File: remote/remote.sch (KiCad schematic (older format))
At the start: 57 parts, among them J1 Conn_01x04, J2 Conn_01x05, Q1 AO3401A, Q2 AO3401A, Q3 AO3401A, Q4 AO3401A, SW1 SW_Push, SW2 SW_Push, SW3 SW_Push, SW4 SW_Push, U1 STM32F030F4Px, U2 RFM69CW-915MHZ

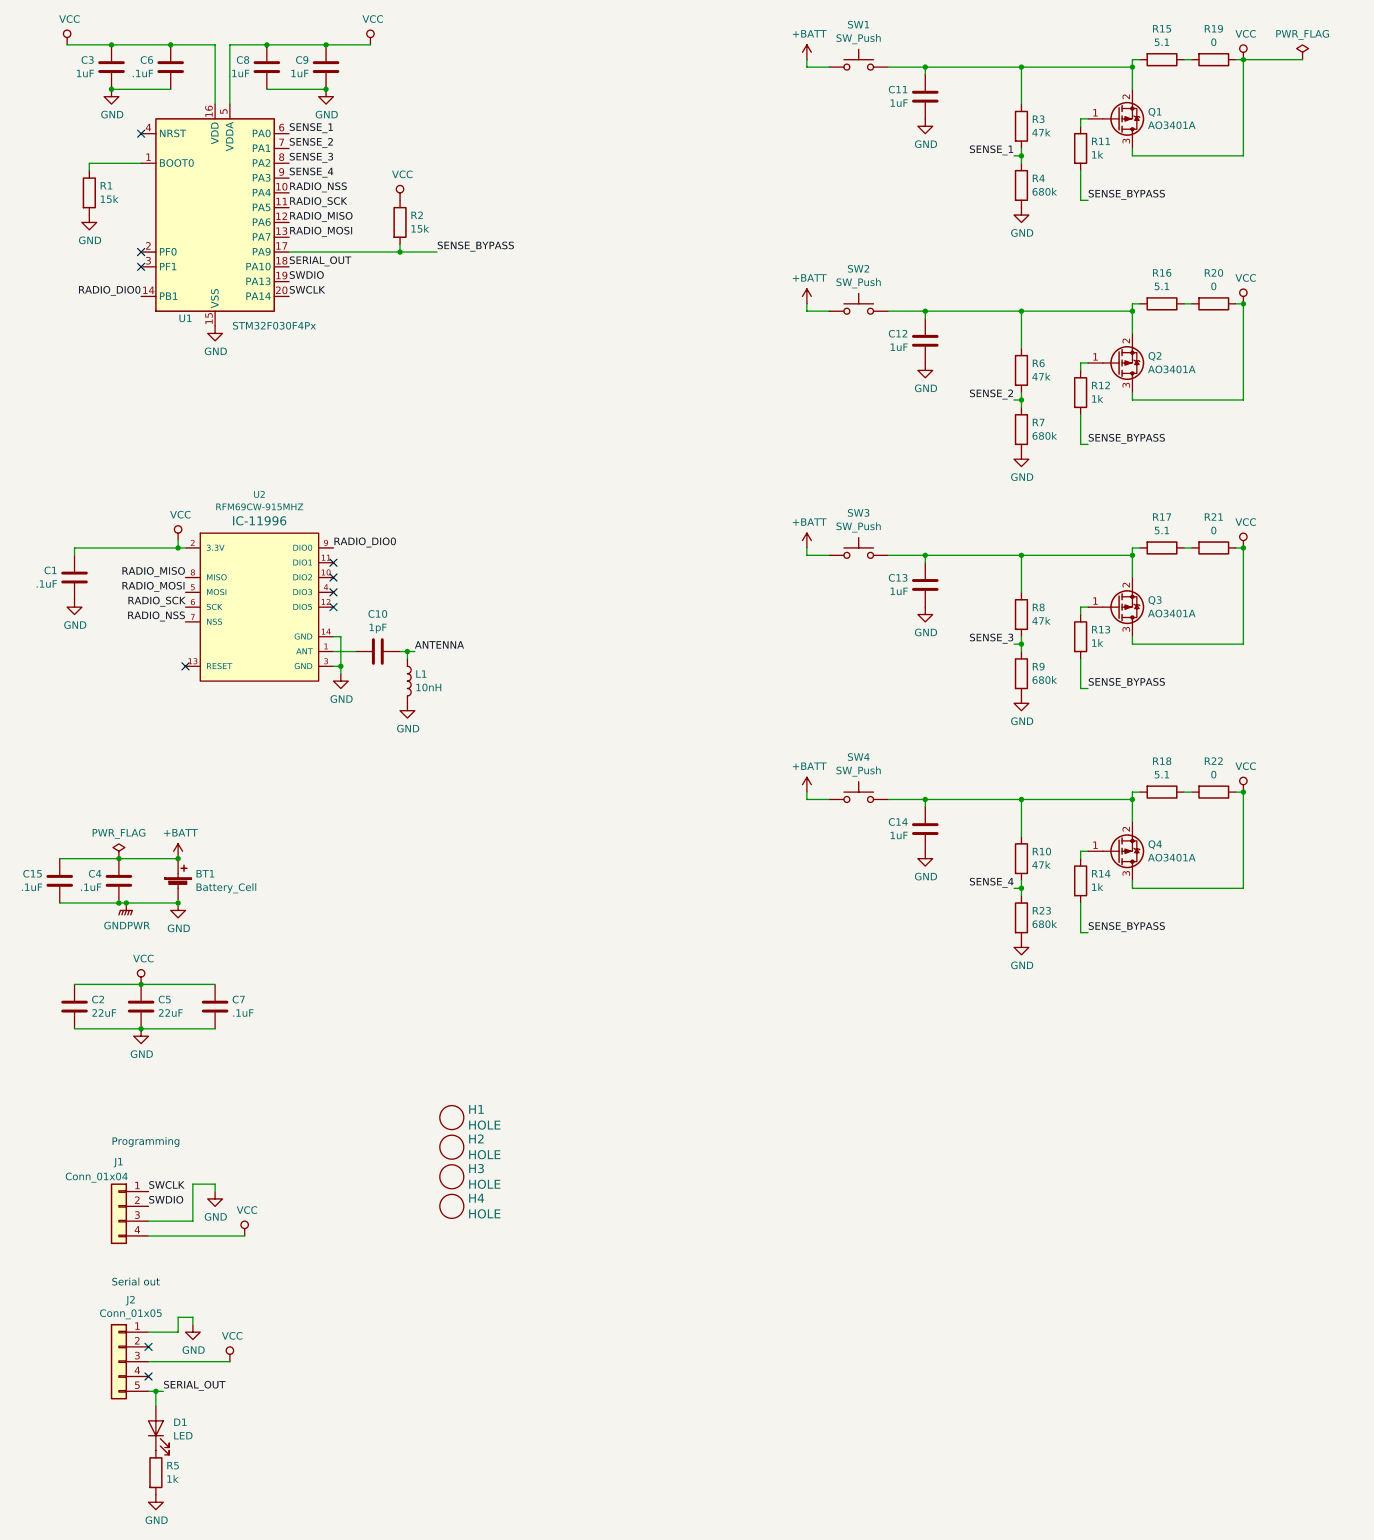
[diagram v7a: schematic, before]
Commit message: Update schematic for hardware v1.1:
- Change to always-on, using interrupts to detect button presses
- Expose pads for easy resetting
- Leave an analog-capable pin unconnected, for random seeding
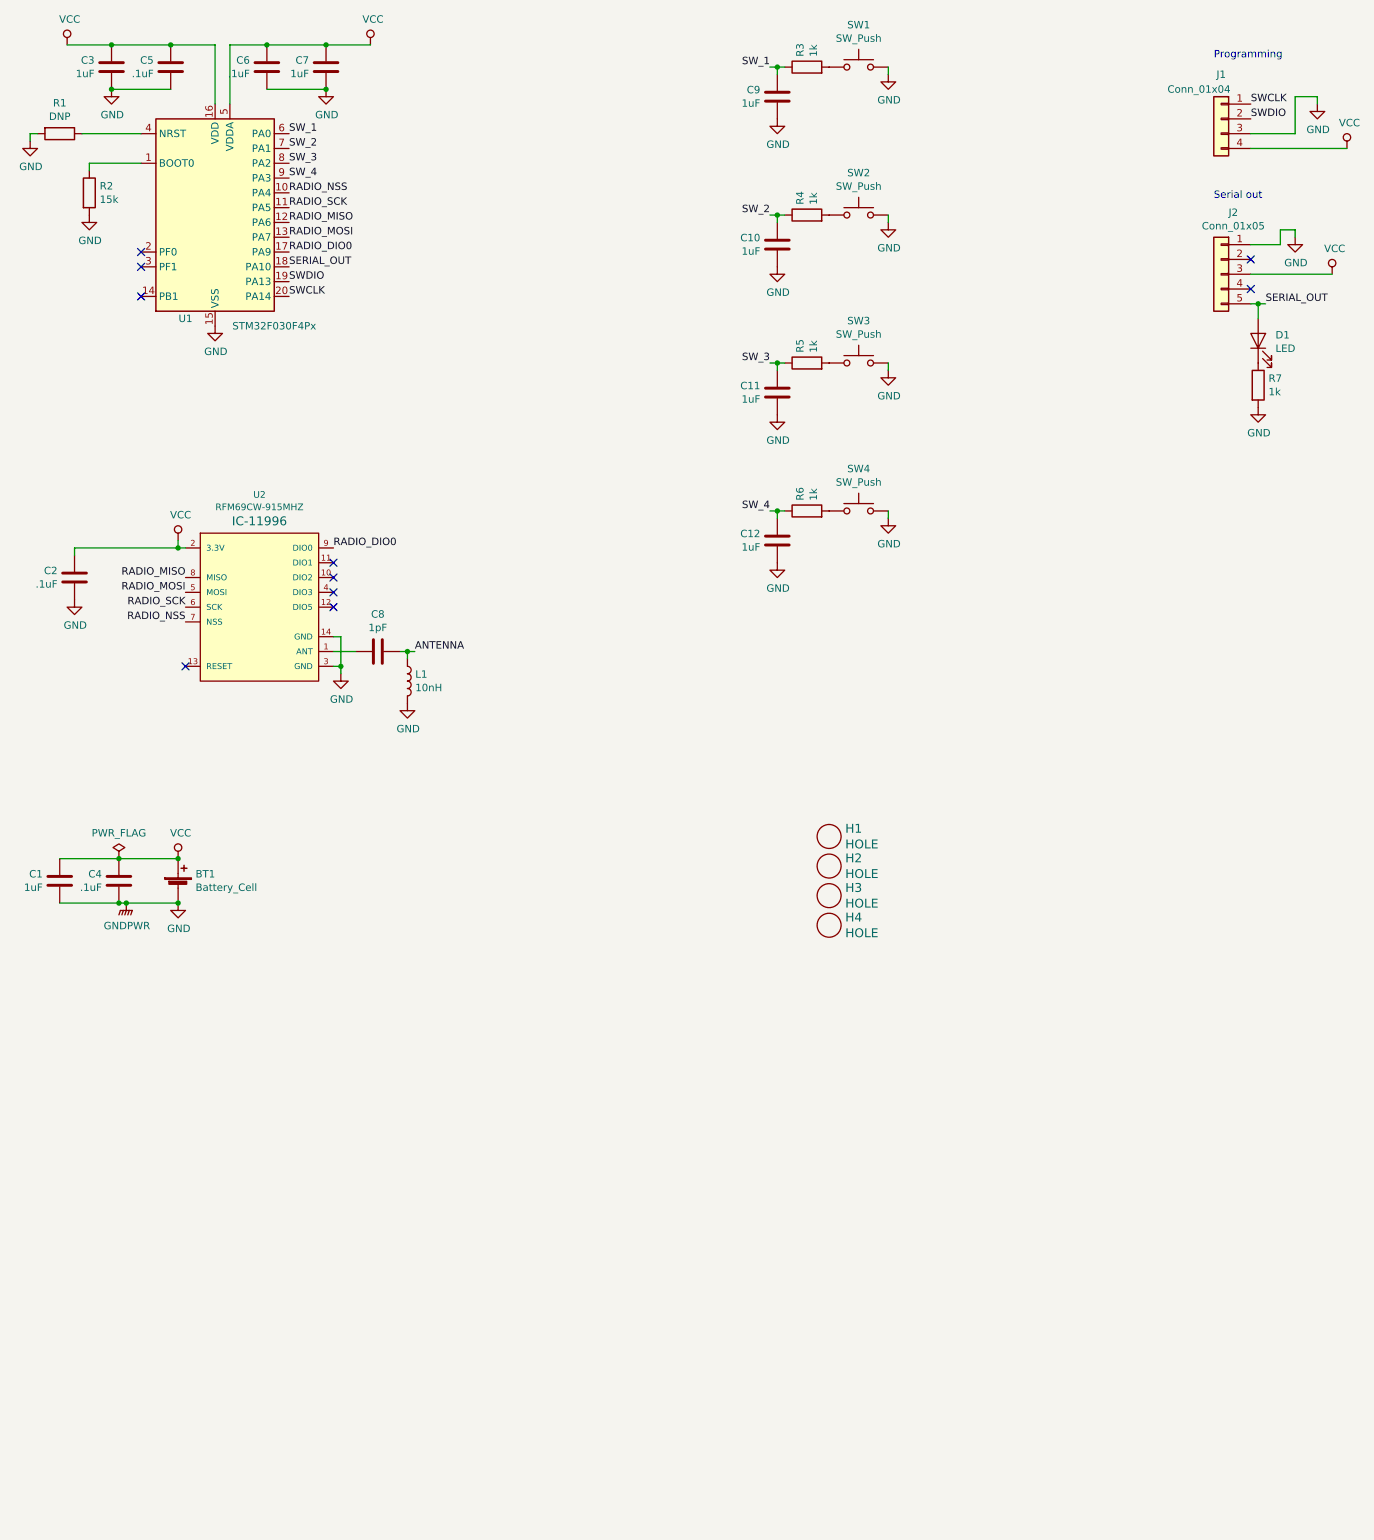
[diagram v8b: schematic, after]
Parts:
- removed C13, C14: 1uF, Capacitor_SMD:C_0402_1005Metric, symbol Device:C
- removed C15, C7: .1uF, Capacitor_SMD:C_0402_1005Metric, symbol Device:C
- removed C2, C5: 22uF, Capacitor_SMD:C_0603_1608Metric, symbol Device:C
- removed Q1, Q2, Q3, Q4: AO3401A, Package_TO_SOT_SMD:SOT-23, symbol Transistor_FET:AO3401A
- removed R10, R8: 47k, Resistor_SMD:R_0402_1005Metric, symbol Device:R
- removed R11, R12, R13, R14: 1k, Resistor_SMD:R_0402_1005Metric, symbol Device:R
- removed R15, R16, R17, R18: 5.1, Resistor_SMD:R_0603_1608Metric, symbol Device:R
- removed R19, R20, R21, R22: 0, Resistor_SMD:R_0603_1608Metric_Pad1.05x0.95mm_HandSolder, symbol Device:R
- removed R2: 15k, Resistor_SMD:R_0402_1005Metric, symbol Device:R
- removed R23, R7, R9: 680k, Resistor_SMD:R_0603_1608Metric, symbol Device:R
- added C1, C10, C11: 1uF, Capacitor_SMD:C_0402_1005Metric, symbol Device:C
- added R1: DNP, Resistor_SMD:R_0805_2012Metric_Pad1.15x1.40mm_HandSolder, symbol Device:R
- added R5: 1k, Resistor_SMD:R_0402_1005Metric, symbol Device:R
- C8: renamed from C10; footprint Capacitor_SMD:C_0603_1608Metric_Pad1.05x0.95mm_HandSolder -> Capacitor_SMD:C_0402_1005Metric; LCSC (none) -> C1550; Part VJ0603A1R0BXACW1BC‎ -> (none)
- L1: footprint Inductor_SMD:L_0603_1608Metric_Pad1.05x0.95mm_HandSolder -> Inductor_SMD:L_0402_1005Metric; LCSC (none) -> C27147; Part BWCS0016100810NG00 -> (none)
- R3, R6: value 47k -> 1k; LCSC C25792 -> C11702
- R4: value 680k -> 1k; footprint Resistor_SMD:R_0603_1608Metric -> Resistor_SMD:R_0402_1005Metric; LCSC C25822 -> C11702
- renumbered C1 to C2, C6 to C5, C8 to C6, C9 to C7, C11 to C9, R1 to R2, R5 to R7
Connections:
- net SENSE_4 is gone; now on net SW_4: U1.9 (PA3)
- net SENSE_BYPASS is gone; now on net RADIO_DIO0: U1.17 (PA9)
- net GND: now also SW1.2, SW2.2, SW3.2, SW4.2, C1.1, C10.1, C11.1, R1.2; no longer R4.2
- net RADIO_DIO0: no longer U1.14 (PB1)
- net VCC: now also BT1.1 (+), C4.2, C1.2
- net at U1.4 (NRST): now also R1.1
- net SW_1: now reaches C9.2, R3.1
- net SW_1: now also U1.6 (PA0); no longer SW1.2
- net SW_4: now reaches C12.2, R6.1
- net SW_4: no longer SW2.2
- removed net +BATT: BT1.1 (+), C4.2, SW1.1, SW2.1, SW3.1, SW4.1
- removed net SENSE_1: R3.2, R4.1, U1.6 (PA0)
- net SENSE_2: no longer names the net of R6.2
- net SENSE_2: now also SW4.1; no longer U1.7 (PA1)
- net SENSE_3 renamed SW_3
- net SW_3: now also C11.2, R5.1
- new net: R3.2, SW1.1
- new net: R4.2, SW2.1
- new net: R5.2, SW3.1
- new net SW_2: C10.2, R4.1, U1.7 (PA1)
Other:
- moved on the sheet: C9, D1, H1, H2, H3, H4, J1, J2, R7
